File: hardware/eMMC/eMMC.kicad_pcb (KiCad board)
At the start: 2 copper layers, 53.3 x 86.4 mm, 9 parts, among them J1 Left, J2 Right, J3 DBG, J4 Left, J5 Right

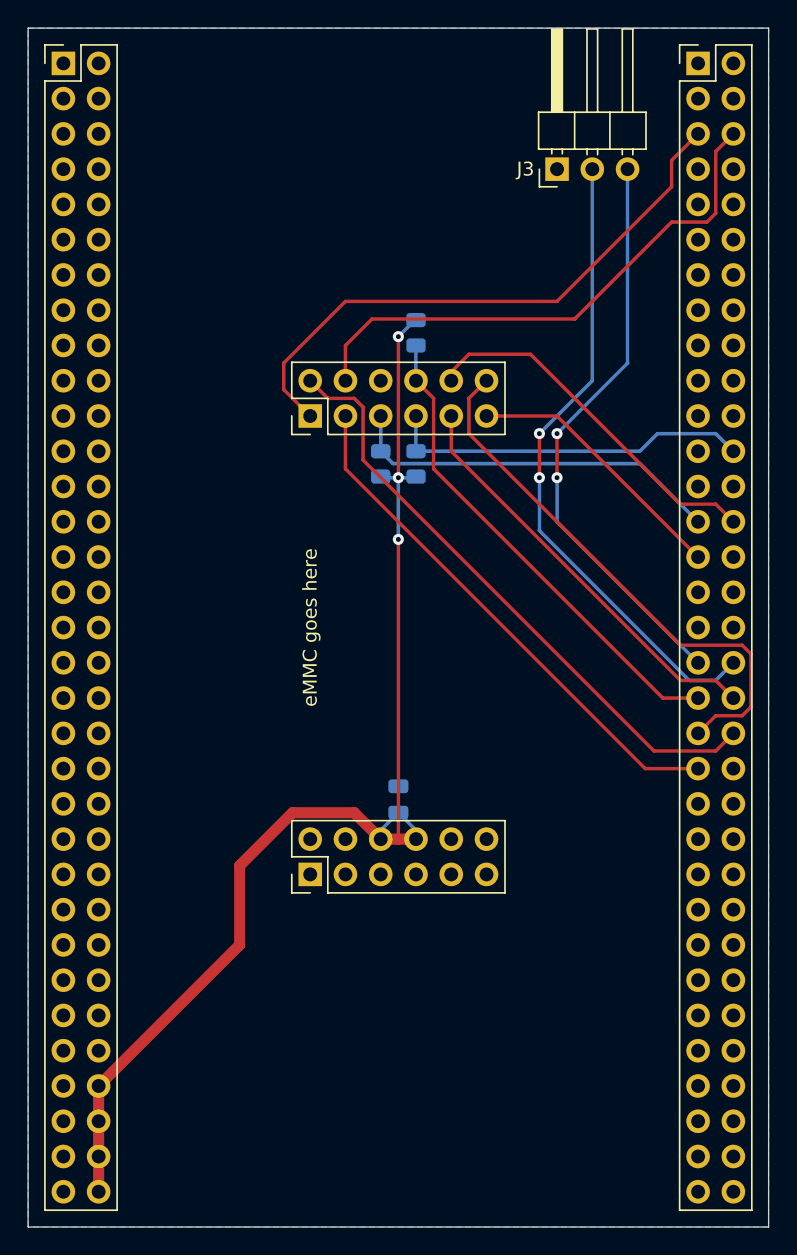
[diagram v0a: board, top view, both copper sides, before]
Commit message: hardware: eMMC top to rev.B
+ Harmonized daughter board orientation

+ Modified J3 DBG to break out SWO and GPIO pins
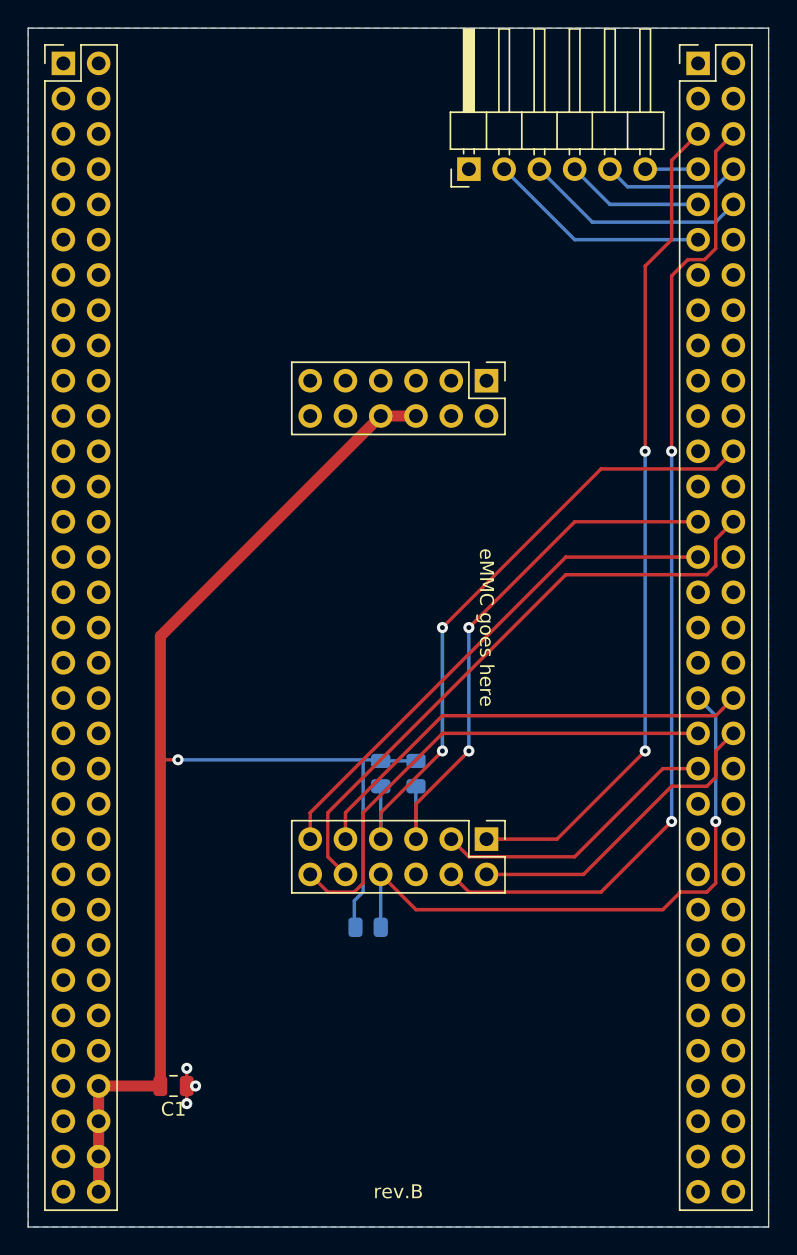
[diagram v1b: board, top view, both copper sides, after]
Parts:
- C1: renamed from C3; moved to F.Cu
- J3: footprint Connector_PinHeader_2.54mm:PinHeader_1x03_P2.54mm_Horizontal -> Connector_PinHeader_2.54mm:PinHeader_1x06_P2.54mm_Horizontal
- moved R1 43.0 mm to (123.5, 113.0), turned to 0 degrees
- moved J4 37.8 mm to (132.1, 73.7), turned to 270 degrees
- moved J5 33.0 mm to (132.1, 106.7), turned to 270 degrees
- moved C1 26.2 mm to (109.5, 124.5), turned to 180 degrees
- moved R2 22.4 mm to (124.5, 102.0), turned to 270 degrees
- moved R3 22.4 mm to (127.0, 102.0), turned to 270 degrees
- moved J3 6.35 mm to (130.8, 58.4)
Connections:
- J1 pad 10: C13 -> (no net)
- J1 pad 11: C14 -> (no net)
- J1 pad 12: C15 -> (no net)
- J1 pad 13: F0 -> (no net)
- J1 pad 14: F1 -> (no net)
- J1 pad 15: F2 -> (no net)
- J1 pad 16: F3 -> (no net)
- J1 pad 17: F4 -> (no net)
- J1 pad 18: F5 -> (no net)
- J1 pad 19: F6 -> (no net)
- J1 pad 20: F7 -> (no net)
- J1 pad 21: F8 -> (no net)
- J1 pad 22: F9 -> (no net)
- J1 pad 23: F10 -> (no net)
- J1 pad 24: C0 -> (no net)
- J1 pad 25: C1 -> (no net)
- J1 pad 26: C2 -> (no net)
- J1 pad 27: C3 -> (no net)
- J1 pad 3: E0 -> (no net)
- J1 pad 32: A4 -> (no net)
- J1 pad 33: A5 -> (no net)
- J1 pad 34: A6 -> (no net)
- J1 pad 35: A7 -> (no net)
- J1 pad 36: C4 -> (no net)
- J1 pad 37: C5 -> (no net)
- J1 pad 38: B0 -> (no net)
- J1 pad 39: B1 -> (no net)
- J1 pad 4: E1 -> (no net)
- J1 pad 40: B2 -> (no net)
- J1 pad 41: F11 -> (no net)
- J1 pad 42: F12 -> (no net)
- J1 pad 43: F13 -> (no net)
- J1 pad 44: F14 -> (no net)
- J1 pad 45: F15 -> (no net)
- J1 pad 46: G0 -> (no net)
- J1 pad 47: G1 -> (no net)
- J1 pad 48: E7 -> (no net)
- J1 pad 49: E8 -> (no net)
- J1 pad 5: E2 -> (no net)
- J1 pad 50: E9 -> (no net)
- J1 pad 51: E10 -> (no net)
- J1 pad 52: E11 -> (no net)
- J1 pad 53: E12 -> (no net)
- J1 pad 54: E13 -> (no net)
- J1 pad 55: E14 -> (no net)
- J1 pad 56: E15 -> (no net)
- J1 pad 57: B10 -> (no net)
- J1 pad 58: B11 -> (no net)
- J1 pad 6: E3 -> (no net)
- J1 pad 7: E4 -> (no net)
- J1 pad 8: E5 -> (no net)
- J1 pad 9: E6 -> (no net)
- J2 pad 1: Net-(J2-Pad1) -> (no net)
- J2 pad 10: B4 -> PB4
- J2 pad 11: B3 -> PB3
- J2 pad 12: G15 -> (no net)
- J2 pad 13: G14 -> (no net)
- J2 pad 14: G13 -> (no net)
- J2 pad 15: G12 -> (no net)
- J2 pad 16: G11 -> (no net)
- J2 pad 17: G10 -> (no net)
- J2 pad 18: G9 -> (no net)
- J2 pad 19: D7 -> (no net)
- J2 pad 20: D6 -> (no net)
- J2 pad 21: D5 -> (no net)
- J2 pad 22: D4 -> (no net)
- J2 pad 23: D3 -> (no net)
- J2 pad 25: D1 -> (no net)
- J2 pad 26: D0 -> (no net)
- J2 pad 3: Net-(J2-Pad3) -> (no net)
- J2 pad 30: A15 -> (no net)
- J2 pad 31: A14 -> (no net)
- J2 pad 32: A13 -> (no net)
- J2 pad 33: A12 -> (no net)
- J2 pad 34: A11 -> (no net)
- J2 pad 35: A10 -> (no net)
- J2 pad 36: A9 -> (no net)
- J2 pad 42: G8 -> (no net)
- J2 pad 43: G7 -> (no net)
- J2 pad 44: G6 -> (no net)
- J2 pad 45: G5 -> (no net)
- J2 pad 46: G4 -> (no net)
- J2 pad 47: G3 -> (no net)
- J2 pad 48: G2 -> (no net)
- J2 pad 49: D15 -> (no net)
- J2 pad 50: D14 -> (no net)
- J2 pad 51: D13 -> (no net)
- J2 pad 52: D12 -> (no net)
- J2 pad 53: D11 -> (no net)
- J2 pad 54: D10 -> (no net)
- J2 pad 55: D9 -> (no net)
- J2 pad 56: D8 -> (no net)
- J2 pad 57: B15 -> (no net)
- J2 pad 58: B14 -> (no net)
- J2 pad 59: B13 -> (no net)
- J2 pad 60: B12 -> (no net)
- J2 pad 65: +5V -> (no net)
- J2 pad 7: B7 -> PB7
- J2 pad 8: B6 -> PB6
- J2 pad 9: B5 -> PB5
- J3 pad 2: A9 -> PB3
- J3 pad 3: A10 -> PB4
- J4 pad 10: Net-(J4-Pad10) -> (no net)
- J4 pad 12: Net-(J4-Pad12) -> (no net)
- J4 pad 2: Net-(J4-Pad2) -> (no net)
- J4 pad 4: Net-(J4-Pad4) -> (no net)
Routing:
- net A9: track 46.6 -> 0.00 mm, vias 2 -> 0
- net A10: track 41.9 -> 0.00 mm, vias 2 -> 0
- net DAT4: track 39.4 -> 70.6 mm, vias 0 -> 2
- net DAT7: track 44.3 -> 23.1 mm
- net CMD: track 26.5 -> 47.1 mm, vias 0 -> 2
- net DAT2: track 19.4 -> 37.5 mm
- net DAT5: track 42.4 -> 60.1 mm, vias 0 -> 2
- net DAT3: track 26.5 -> 44.0 mm
- net DAT6: track 38.2 -> 20.9 mm
- net PB4: track 0.00 -> 16.1 mm
- net PB3: track 0.00 -> 16.1 mm
- net CLK: track 27.5 -> 40.3 mm, vias 0 -> 2
- net +3V3: track 88.2 -> 100.2 mm, vias 3 -> 1
- net PB6: track 0.00 -> 9.94 mm
- net PB5: track 0.00 -> 9.94 mm
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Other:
- board text added: "rev.B"

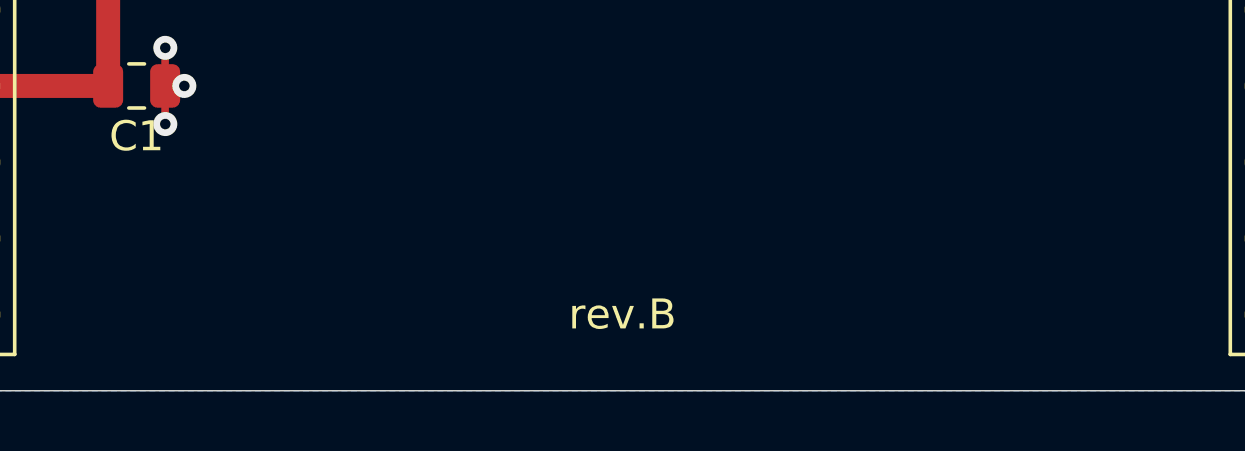
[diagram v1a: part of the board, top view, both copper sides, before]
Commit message: hardware: update top board labels
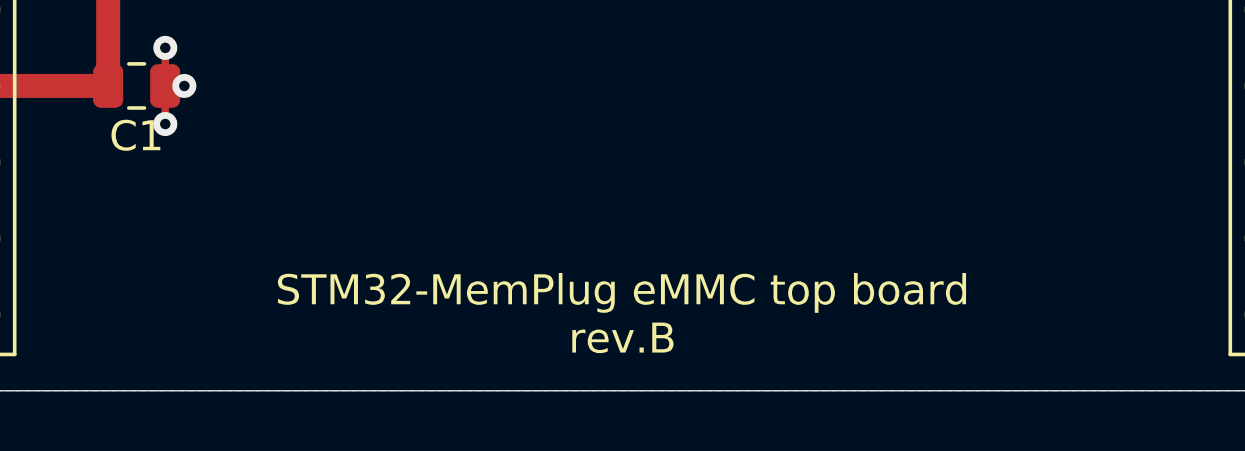
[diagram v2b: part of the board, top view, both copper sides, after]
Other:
- board text added: "STM32-MemPlug eMMC top board rev.B"
- board text removed: "rev.B"

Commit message: refreshed carrier boards and added missing symbol libs
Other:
- board text added: "DBG1"
- board text added: "DBG2"
- board text added: "DBG3"
- board text added: "DBG4"
- board text added: "GND"
- board text added: "SWO"
